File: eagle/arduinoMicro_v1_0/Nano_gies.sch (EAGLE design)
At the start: 18 parts, among them Q1 BSS138LT1, Q2 BSS138LT1, Q3 BUZ10

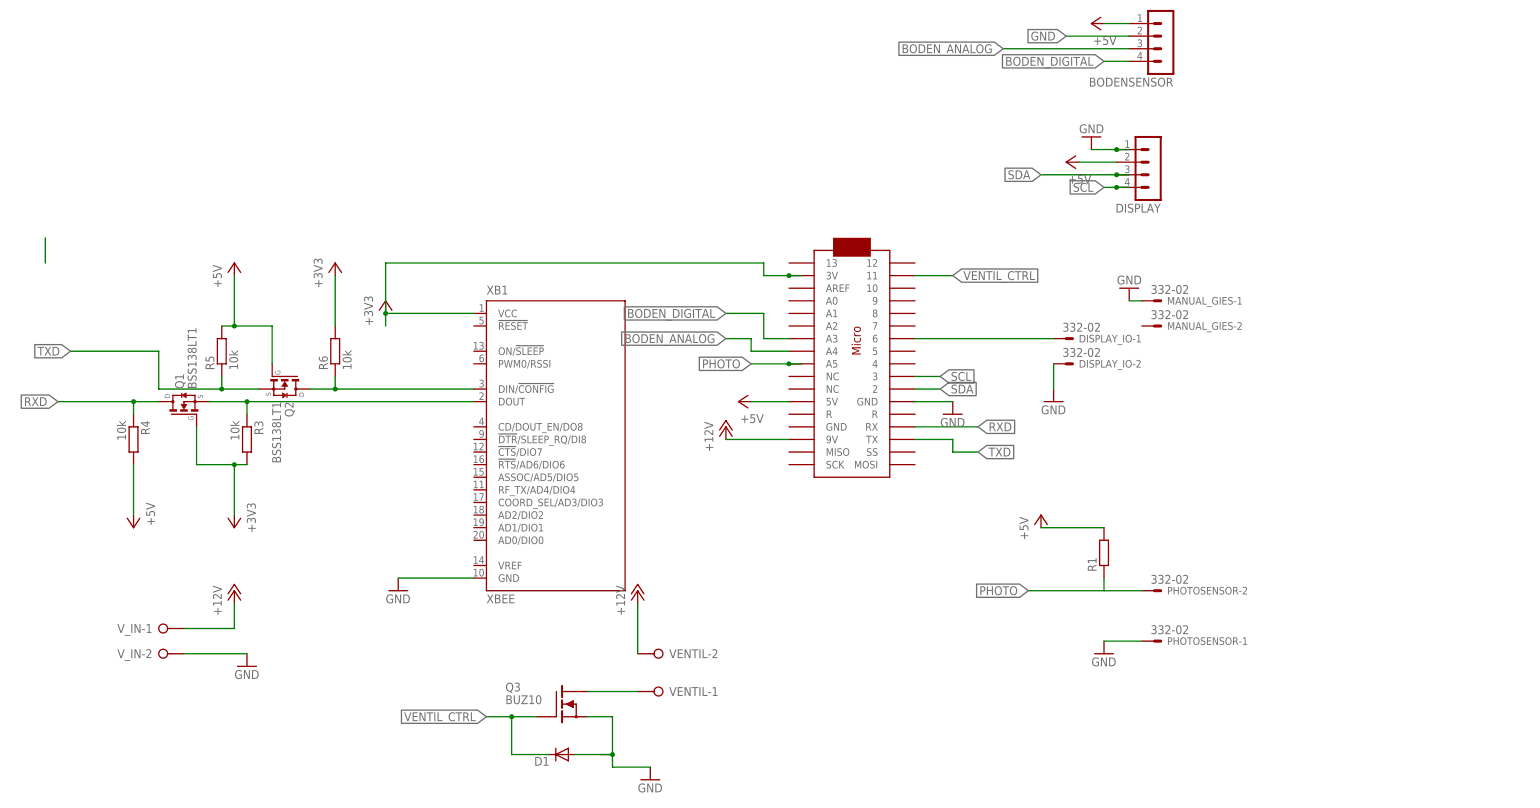
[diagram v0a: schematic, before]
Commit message: Anpassung eagel Files für Grafiken für die Doku. Bilder in Doku eingefügt
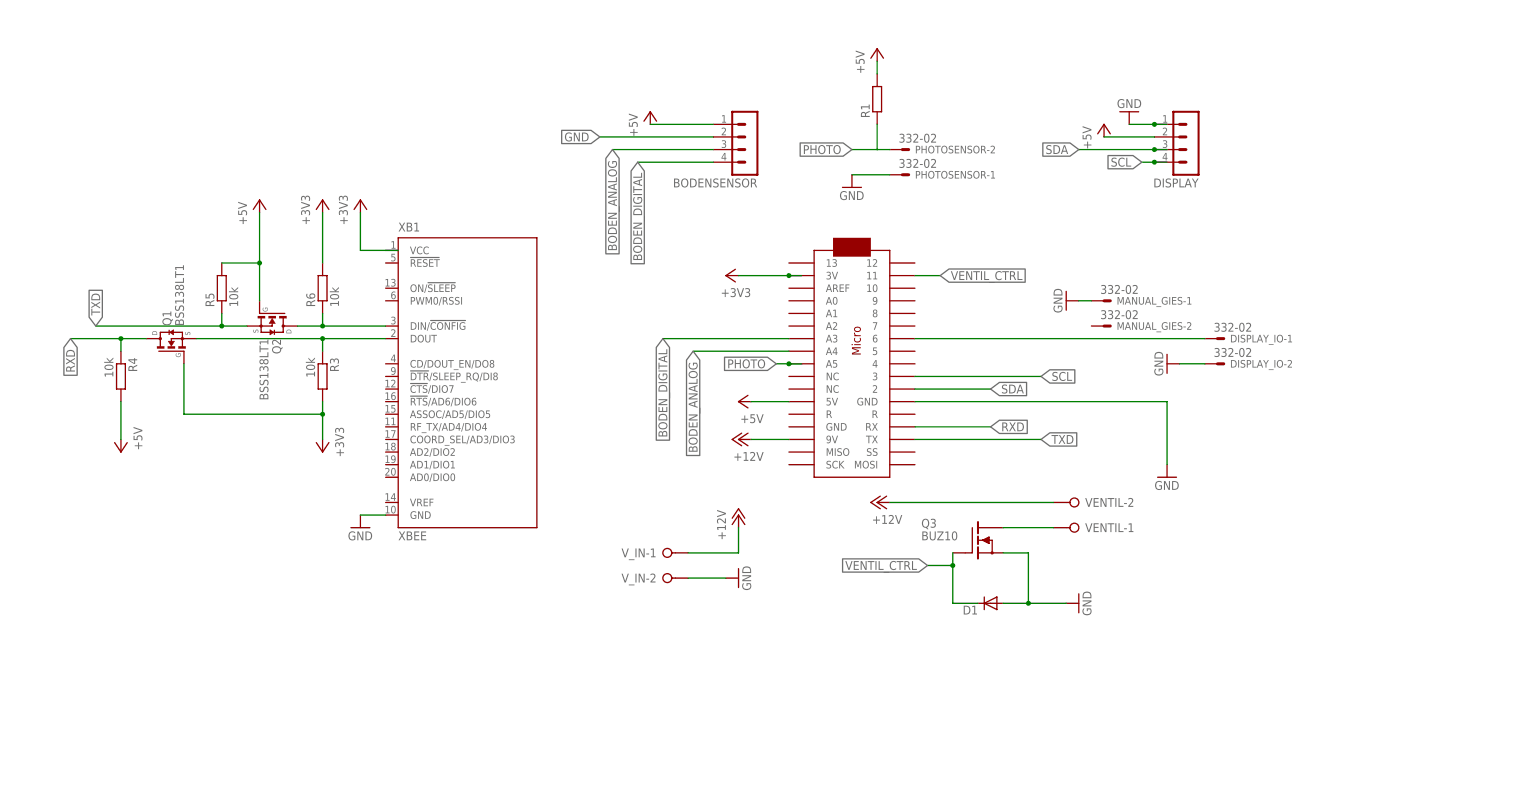
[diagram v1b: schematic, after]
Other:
- moved on the sheet: BODENSENSOR, D1, DISPLAY, DISPLAY_IO-1, DISPLAY_IO-2, MANUAL_GIES-1, MANUAL_GIES-2, PHOTOSENSOR-1, PHOTOSENSOR-2, Q1, Q2, Q3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

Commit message: anpassung der Fehler im Schaltplan beim Anschluss XBee zum Mikrocontroller
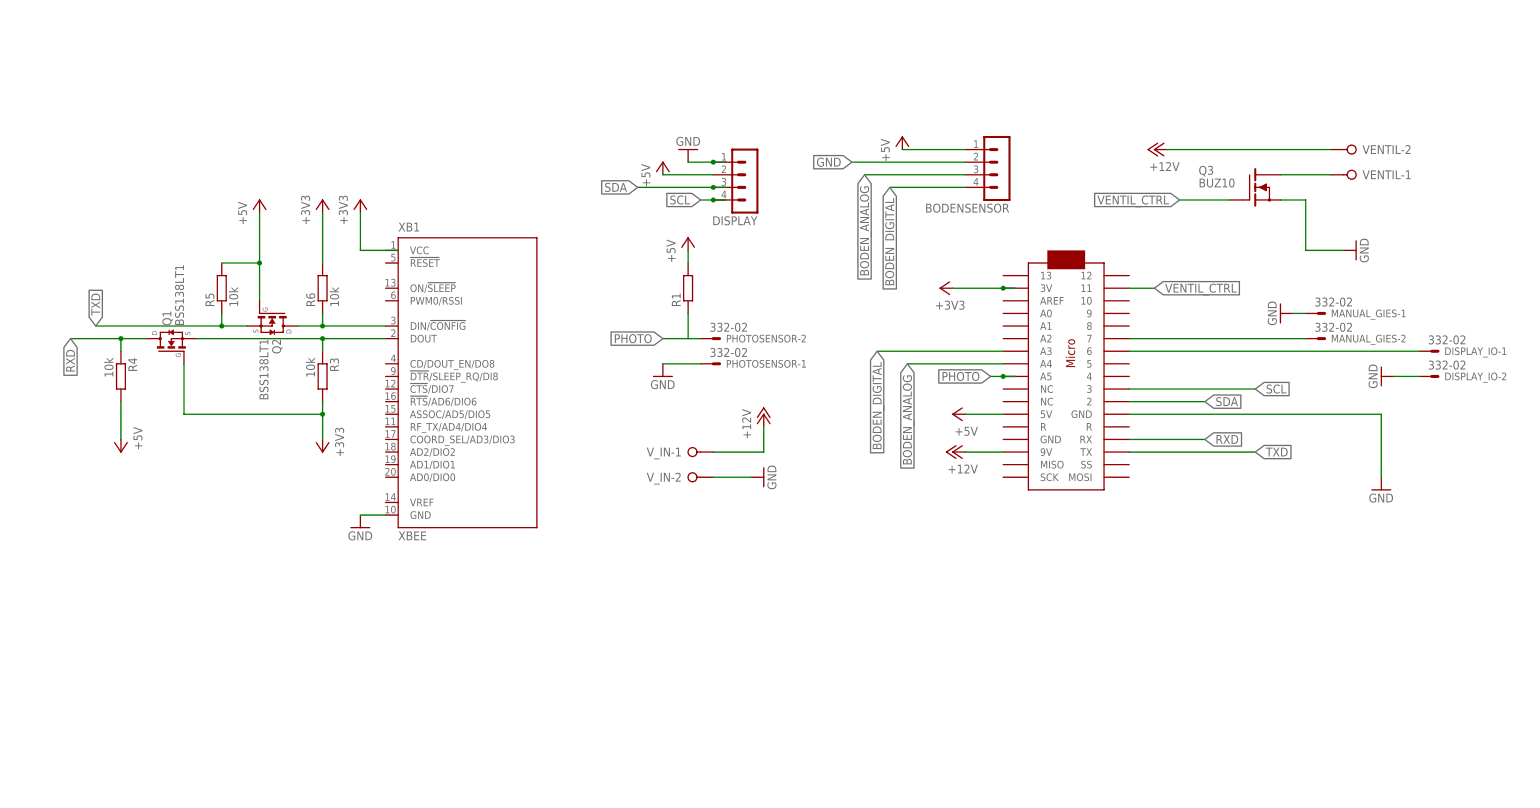
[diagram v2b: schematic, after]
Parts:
- removed D1: (no value), diode:DIODE-DO214AC
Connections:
- new net N$1: MANUAL_GIES-2.S, U$1.7
- net GND: no longer D1.A
- net VENTIL_CTRL: no longer D1.C
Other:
- moved on the sheet: BODENSENSOR, DISPLAY, DISPLAY_IO-1, DISPLAY_IO-2, MANUAL_GIES-1, MANUAL_GIES-2, PHOTOSENSOR-1, PHOTOSENSOR-2, Q3, R1, VENTIL-1, VENTIL-2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
